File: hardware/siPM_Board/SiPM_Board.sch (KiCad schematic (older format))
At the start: 24 parts, among them J1 Conn_02x34_Odd_Even, J2 Conn_02x34_Odd_Even, U1 LM94021, U2 S14161-6050HS-04, U3 S14161-6050HS-04, U4 S14161-6050HS-04, U5 S14161-6050HS-04

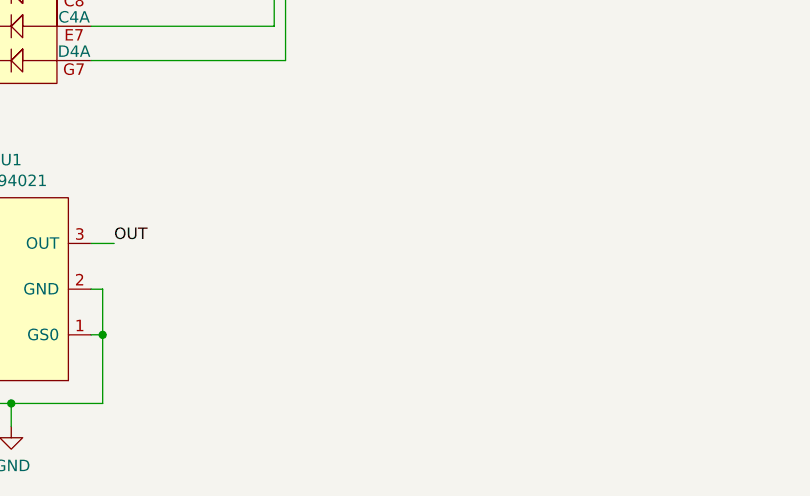
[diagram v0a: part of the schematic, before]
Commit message: Branch to add PEM nuts to SiPM board
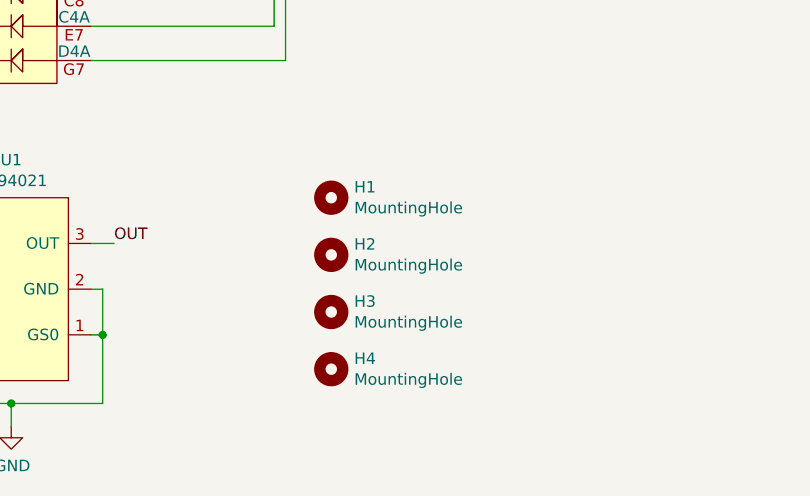
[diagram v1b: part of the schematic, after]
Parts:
- added H1, H2, H3, H4: MountingHole, Arich_SiPM_Footprints:SMTSO-nut-0-80, symbol Mechanical:MountingHole
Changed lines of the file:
@@
 Wire Wire Line
 	6250 4050 6400 4050
+$Comp
+L Mechanical:MountingHole H1
+U 1 1 60E18C43
+P 4500 6500
+F 0 "H1" H 4600 6546 50  0000 L CNN
+F 1 "MountingHole" H 4600 6455 50  0000 L CNN
+F 2 "Arich_SiPM_Footprints:SMTSO-nut-0-80" H 4500 6500 50  0001 C CNN
+F 3 "~" H 4500 6500 50  0001 C CNN
+	1    4500 6500
+	1    0    0    -1
+$EndComp
+$Comp
+L Mechanical:MountingHole H2
+U 1 1 60E1B16D
+P 4500 6750
+F 0 "H2" H 4600 6796 50  0000 L CNN
+F 1 "MountingHole" H 4600 6705 50  0000 L CNN
+F 2 "Arich_SiPM_Footprints:SMTSO-nut-0-80" H 4500 6750 50  0001 C CNN
+F 3 "~" H 4500 6750 50  0001 C CNN
+	1    4500 6750
+	1    0    0    -1
+$EndComp
+$Comp
+L Mechanical:MountingHole H3
+U 1 1 60E1BBA7
+P 4500 7000
+F 0 "H3" H 4600 7046 50  0000 L CNN
+F 1 "MountingHole" H 4600 6955 50  0000 L CNN
+F 2 "Arich_SiPM_Footprints:SMTSO-nut-0-80" H 4500 7000 50  0001 C CNN
+F 3 "~" H 4500 7000 50  0001 C CNN
+	1    4500 7000
+	1    0    0    -1
+$EndComp
+$Comp
+L Mechanical:MountingHole H4
+U 1 1 60E1C52C
+P 4500 7250
+F 0 "H4" H 4600 7296 50  0000 L CNN
+F 1 "MountingHole" H 4600 7205 50  0000 L CNN
+F 2 "Arich_SiPM_Footprints:SMTSO-nut-0-80" H 4500 7250 50  0001 C CNN
+F 3 "~" H 4500 7250 50  0001 C CNN
+	1    4500 7250
+	1    0    0    -1
+$EndComp
 $EndSCHEMATC
